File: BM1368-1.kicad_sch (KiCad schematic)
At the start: 39 parts, among them U10 BM1368_mode1, U11 BM1368_mode1

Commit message: DRC Check
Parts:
- removed R50: 10k, Resistor_SMD:R_0805_2012Metric, symbol Device:R
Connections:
- net U11-VDD1_1: now reaches C85.2, C93.1, U11.28 (VDD1_1)
- net U11-VDD2_1: now reaches C80.2, C85.1, U11.29 (VDD2_1)
- net U11-VDD3_1: now reaches C79.2, C80.1, U11.30 (VDD3_1)
- net Net-(U9-VDD1_1) renamed U9-VDD1_1
- net Net-(U9-VDD2_1) renamed U9-VDD2_1
- net Net-(U9-VDD3_1) renamed U9-VDD3_1
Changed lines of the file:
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@@
 	)
 	(junction
+		(at 67.31 48.26)
+		(diameter 0)
+		(color 0 0 0 0)
+	)
+	(junction
+		(at 234.95 45.72)
+		(diameter 0)
+		(color 0 0 0 0)
+	)
+	(junction
 		(at 78.74 76.2)
 		(diameter 0)
@@
 	)
 	(junction
-		(at 254 55.88)
-		(diameter 0)
-		(color 0 0 0 0)
-	)
-	(junction
 		(at 195.58 45.72)
 		(diameter 0)
@@
 	)
 	(junction
+		(at 257.81 50.8)
+		(diameter 0)
+		(color 0 0 0 0)
+	)
+	(junction
 		(at 118.11 76.2)
 		(diameter 0)
@@
 	)
 	(junction
+		(at 246.38 48.26)
+		(diameter 0)
+		(color 0 0 0 0)
+	)
+	(junction
 		(at 260.35 60.96)
 		(diameter 0)
@@
 	)
 	(junction
+		(at 54.61 50.8)
+		(diameter 0)
+		(color 0 0 0 0)
+	)
+	(junction
 		(at 129.54 48.26)
 		(diameter 0)
@@
 	)
 	(junction
+		(at 77.47 45.72)
+		(diameter 0)
+		(color 0 0 0 0)
+	)
+	(junction
 		(at 195.58 53.34)
 		(diameter 0)
@@
 	(wire
 		(pts
-			(xy 254 55.88) (xy 254 77.47)
-		)
-		(stroke
-			(width 0)
-			(type default)
-		)
-	)
-	(wire
-		(pts
 			(xy 97.79 34.29) (xy 97.79 36.83)
 		)
@@
 	(wire
 		(pts
+			(xy 33.02 45.72) (xy 77.47 45.72)
+		)
+		(stroke
+			(width 0)
+			(type default)
+		)
+	)
+	(wire
+		(pts
 			(xy 161.29 53.34) (xy 195.58 53.34)
 		)
@@
 	(wire
 		(pts
-			(xy 254 55.88) (xy 274.32 55.88)
+			(xy 232.41 55.88) (xy 274.32 55.88)
 		)
 		(stroke
@@
 	(wire
 		(pts
+			(xy 33.02 50.8) (xy 54.61 50.8)
+		)
+		(stroke
+			(width 0)
+			(type default)
+		)
+	)
+	(wire
+		(pts
 			(xy 232.41 66.04) (xy 266.7 66.04)
 		)
@@
 	(wire
 		(pts
+			(xy 246.38 48.26) (xy 278.13 48.26)
+		)
+		(stroke
+			(width 0)
+			(type default)
+		)
+	)
+	(wire
+		(pts
 			(xy 139.7 76.2) (xy 139.7 78.74)
 		)
@@
 	(wire
 		(pts
-			(xy 254 85.09) (xy 254 87.63)
-		)
-		(stroke
-			(width 0)
-			(type default)
-		)
-	)
-	(wire
-		(pts
 			(xy 170.18 36.83) (xy 172.72 36.83)
 		)
@@
 	(wire
 		(pts
+			(xy 33.02 48.26) (xy 67.31 48.26)
+		)
+		(stroke
+			(width 0)
+			(type default)
+		)
+	)
+	(wire
+		(pts
+			(xy 257.81 50.8) (xy 278.13 50.8)
+		)
+		(stroke
+			(width 0)
+			(type default)
+		)
+	)
+	(wire
+		(pts
 			(xy 53.34 36.83) (xy 54.61 36.83)
 		)
@@
 	(wire
 		(pts
-			(xy 232.41 55.88) (xy 254 55.88)
-		)
-		(stroke
-			(width 0)
-			(type default)
-		)
-	)
-	(wire
-		(pts
 			(xy 60.96 58.42) (xy 80.01 58.42)
 		)
@@
 	(wire
 		(pts
+			(xy 234.95 45.72) (xy 278.13 45.72)
+		)
+		(stroke
+			(width 0)
+			(type default)
+		)
+	)
+	(wire
+		(pts
 			(xy 62.23 55.88) (xy 80.01 55.88)
 		)
@@
 		)
 	)
-	(label "Net-(U9-VDD3_1)"
-		(at 77.47 41.91 0)
+	(hierarchical_label "U11-VDD1_1"
+		(shape output)
+		(at 278.13 50.8 0)
 		(fields_autoplaced yes)
 		(effects
@@
 				(size 1.27 1.27)
 			)
-			(justify left bottom)
+			(justify left)
 		)
 	)
-	(label "Net-(U9-VDD2_1)"
-		(at 67.31 48.26 0)
+	(hierarchical_label "U9-VDD1_1"
+		(shape input)
+		(at 33.02 50.8 180)
 		(fields_autoplaced yes)
 		(effects
@@
 				(size 1.27 1.27)
 			)
-			(justify left bottom)
+			(justify right)
 		)
 	)
-	(label "Net-(U9-VDD1_1)"
-		(at 55.88 50.8 0)
+	(hierarchical_label "U9-VDD2_1"
+		(shape input)
+		(at 33.02 48.26 180)
 		(fields_autoplaced yes)
 		(effects
@@
 				(size 1.27 1.27)
 			)
-			(justify left bottom)
+			(justify right)
 		)
 	)
@@
 		)
 	)
+	(hierarchical_label "U11-VDD3_1"
+		(shape output)
+		(at 278.13 45.72 0)
+		(fields_autoplaced yes)
+		(effects
+			(font
+				(size 1.27 1.27)
+			)
+			(justify left)
+		)
+	)
 	(hierarchical_label "BI"
 		(shape input)
@@
 		)
 	)
+	(hierarchical_label "U11-VDD2_1"
+		(shape output)
+		(at 278.13 48.26 0)
+		(fields_autoplaced yes)
+		(effects
+			(font
+				(size 1.27 1.27)
+			)
+			(justify left)
+		)
+	)
 	(hierarchical_label "BO"
 		(shape output)
@@
 		)
 	)
+	(hierarchical_label "U9-VDD3_1"
+		(shape input)
+		(at 33.02 45.72 180)
+		(fields_autoplaced yes)
+		(effects
+			(font
+				(size 1.27 1.27)
+			)
+			(justify right)
+		)
+	)
 	(hierarchical_label "CLKI"
 		(shape input)
@@
 	)
 	(symbol
-		(lib_id "Device:R")
-		(at 254 81.28 0)
-		(unit 1)
-		(exclude_from_sim no)
-		(in_bom yes)
-		(on_board yes)
-		(dnp no)
-		(property "Reference" "R50"
-			(at 251.714 80.772 90)
-			(effects
-				(font
-					(size 1.27 1.27)
-				)
-			)
-		)
-		(property "Value" "10k"
-			(at 255.905 80.645 90)
-			(effects
-				(font
-					(size 1.27 1.27)
-				)
-			)
-		)
-		(property "Footprint" "Resistor_SMD:R_0805_2012Metric"
-			(at 252.222 81.28 90)
-			(effects
-				(font
-					(size 1.27 1.27)
-				)
-				(hide yes)
-			)
-		)
-		(property "Datasheet" "~"
-			(at 254 81.28 0)
-			(effects
-				(font
-					(size 1.27 1.27)
-				)
-				(hide yes)
-			)
-		)
-		(property "Description" ""
-			(at 254 81.28 0)
-			(effects
-				(font
-					(size 1.27 1.27)
-				)
-				(hide yes)
-			)
-		)
-		(pin "1"
-		)
-		(pin "2"
-		)
-		(instances
-			(project "Nerd8"
-				(path "/e63e39d7-6ac0-4ffd-8aa3-1841a4541b55/4cf9c075-d009-4c35-9949-adda70ae20c7/65deb7aa-d17b-462a-abf5-da4343664945"
-					(reference "R50")
-					(unit 1)
-				)
-			)
-		)
-	)
-	(symbol
 		(lib_id "Device:C")
 		(at 60.96 36.83 90)
@@
 					(unit 1)
 				)
-			)
-		)
-	)
-	(symbol
-		(lib_id "power:+1V8")
-		(at 254 87.63 180)
-		(unit 1)
-		(exclude_from_sim no)
-		(in_bom yes)
-		(on_board yes)
-		(dnp no)
-		(property "Reference" "#PWR0364"
-			(at 254 83.82 0)
-			(effects
-				(font
-					(size 1.27 1.27)
-				)
-				(hide yes)
-			)
-		)
-		(property "Value" "GND"
-			(at 254 92.71 90)
-			(effects
-				(font
-					(size 1.27 1.27)
-				)
-			)
-		)
-		(property "Footprint" ""
-			(at 254 87.63 0)
-			(effects
-				(font
-					(size 1.27 1.27)
-				)
-				(hide yes)
-			)
-		)
-		(property "Datasheet" ""
-			(at 254 87.63 0)
-			(effects
-				(font
-					(size 1.27 1.27)
-				)
-				(hide yes)
-			)
-		)
-		(property "Description" ""
-			(at 254 87.63 0)
-			(effects
-				(font
-					(size 1.27 1.27)
-				)
-				(hide yes)
-			)
-		)
-		(pin "1"
-		)
-		(instances
-			(project "Nerd8"
-				(path "/e63e39d7-6ac0-4ffd-8aa3-1841a4541b55/4cf9c075-d009-4c35-9949-adda70ae20c7/65deb7aa-d17b-462a-abf5-da4343664945"
-					(reference "#PWR0364")
-					(unit 1)
-				)

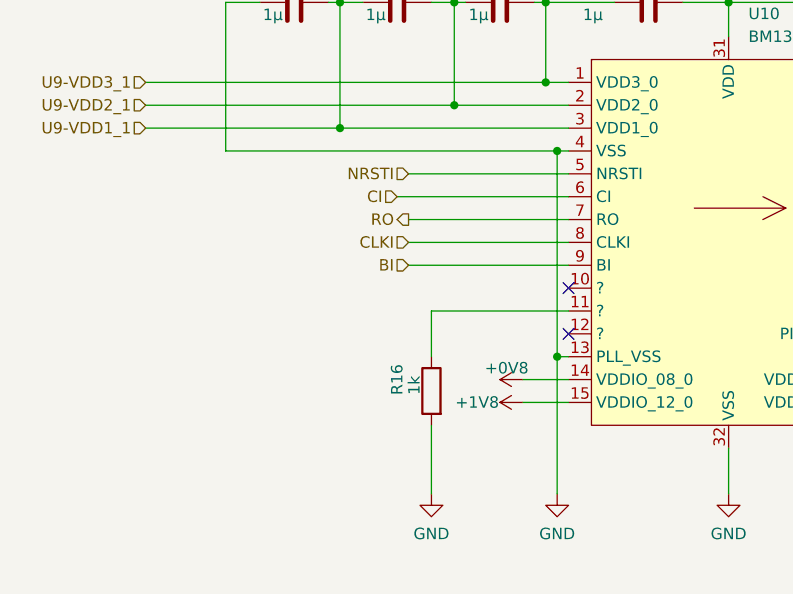
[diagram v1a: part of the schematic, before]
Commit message: References and Logos
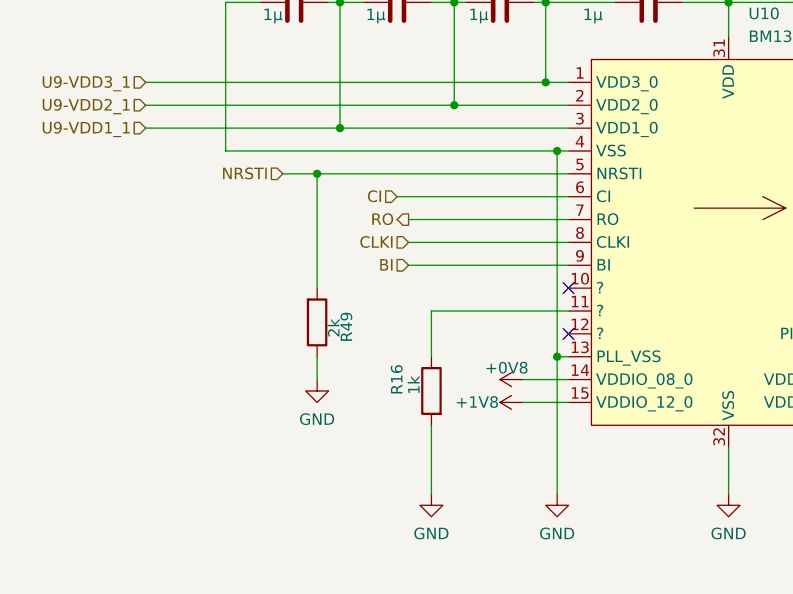
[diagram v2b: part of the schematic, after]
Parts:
- added R49: 2k, Resistor_SMD:R_0805_2012Metric, symbol Device:R
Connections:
- net GND: now also R49.1
- net NRSTI: now also R49.2
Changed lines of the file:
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@@
 	)
 	(junction
+		(at 52.07 55.88)
+		(diameter 0)
+		(color 0 0 0 0)
+	)
+	(junction
 		(at 195.58 36.83)
 		(diameter 0)
@@
 	(wire
 		(pts
+			(xy 52.07 76.2) (xy 52.07 78.74)
+		)
+		(stroke
+			(width 0)
+			(type default)
+		)
+	)
+	(wire
+		(pts
 			(xy 115.57 53.34) (xy 118.11 53.34)
 		)
@@
 	(wire
 		(pts
+			(xy 52.07 55.88) (xy 52.07 68.58)
+		)
+		(stroke
+			(width 0)
+			(type default)
+		)
+	)
+	(wire
+		(pts
 			(xy 118.11 45.72) (xy 118.11 36.83)
 		)
@@
 	(wire
 		(pts
+			(xy 52.07 55.88) (xy 80.01 55.88)
+		)
+		(stroke
+			(width 0)
+			(type default)
+		)
+	)
+	(wire
+		(pts
 			(xy 54.61 50.8) (xy 80.01 50.8)
 		)
@@
 	(wire
 		(pts
-			(xy 62.23 55.88) (xy 80.01 55.88)
+			(xy 48.26 55.88) (xy 52.07 55.88)
 		)
 		(stroke
@@
 	(hierarchical_label "NRSTI"
 		(shape input)
-		(at 62.23 55.88 180)
+		(at 48.26 55.88 180)
 		(fields_autoplaced yes)
 		(effects
@@
 	)
 	(symbol
+		(lib_id "Device:R")
+		(at 52.07 72.39 0)
+		(mirror x)
+		(unit 1)
+		(exclude_from_sim no)
+		(in_bom yes)
+		(on_board yes)
+		(dnp no)
+		(property "Reference" "R49"
+			(at 55.372 72.898 90)
+			(effects
+				(font
+					(size 1.27 1.27)
+				)
+			)
+		)
+		(property "Value" "2k"
+			(at 53.975 73.025 90)
+			(effects
+				(font
+					(size 1.27 1.27)
+				)
+			)
+		)
+		(property "Footprint" "Resistor_SMD:R_0805_2012Metric"
+			(at 50.292 72.39 90)
+			(effects
+				(font
+					(size 1.27 1.27)
+				)
+				(hide yes)
+			)
+		)
+		(property "Datasheet" "~"
+			(at 52.07 72.39 0)
+			(effects
+				(font
+					(size 1.27 1.27)
+				)
+				(hide yes)
+			)
+		)
+		(property "Description" ""
+			(at 52.07 72.39 0)
+			(effects
+				(font
+					(size 1.27 1.27)
+				)
+				(hide yes)
+			)
+		)
+		(pin "1"
+		)
+		(pin "2"
+		)
+		(instances
+			(project "Nerd8"
+				(path "/e63e39d7-6ac0-4ffd-8aa3-1841a4541b55/4cf9c075-d009-4c35-9949-adda70ae20c7/65deb7aa-d17b-462a-abf5-da4343664945"
+					(reference "R49")
+					(unit 1)
+				)
+			)
+		)
+	)
+	(symbol
 		(lib_name "GND_7")
 		(lib_id "power:GND")
@@
 					(unit 1)
 				)
+			)
+		)
+	)
+	(symbol
+		(lib_id "power:GND")
+		(at 52.07 78.74 0)
+		(mirror y)
+		(unit 1)
+		(exclude_from_sim no)
+		(in_bom yes)
+		(on_board yes)
+		(dnp no)
+		(fields_autoplaced yes)
+		(property "Reference" "#PWR0339"
+			(at 52.07 85.09 0)
+			(effects
+				(font
+					(size 1.27 1.27)
+				)
+				(hide yes)
+			)
+		)
+		(property "Value" "GND"
+			(at 52.07 83.185 0)
+			(effects
+				(font
+					(size 1.27 1.27)
+				)
+			)
+		)
+		(property "Footprint" ""
+			(at 52.07 78.74 0)
+			(effects
+				(font
+					(size 1.27 1.27)
+				)
+				(hide yes)
+			)
+		)
+		(property "Datasheet" ""
+			(at 52.07 78.74 0)
+			(effects
+				(font
+					(size 1.27 1.27)
+				)
+				(hide yes)
+			)
+		)
+		(property "Description" ""
+			(at 52.07 78.74 0)
+			(effects
+				(font
+					(size 1.27 1.27)
+				)
+				(hide yes)
+			)
+		)
+		(pin "1"
+		)
+		(instances
+			(project "Nerd8"
+				(path "/e63e39d7-6ac0-4ffd-8aa3-1841a4541b55/4cf9c075-d009-4c35-9949-adda70ae20c7/65deb7aa-d17b-462a-abf5-da4343664945"
+					(reference "#PWR0339")
+					(unit 1)
+				)
